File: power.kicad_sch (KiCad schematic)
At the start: 1 part, among them U4 LX7167ACLD-TR

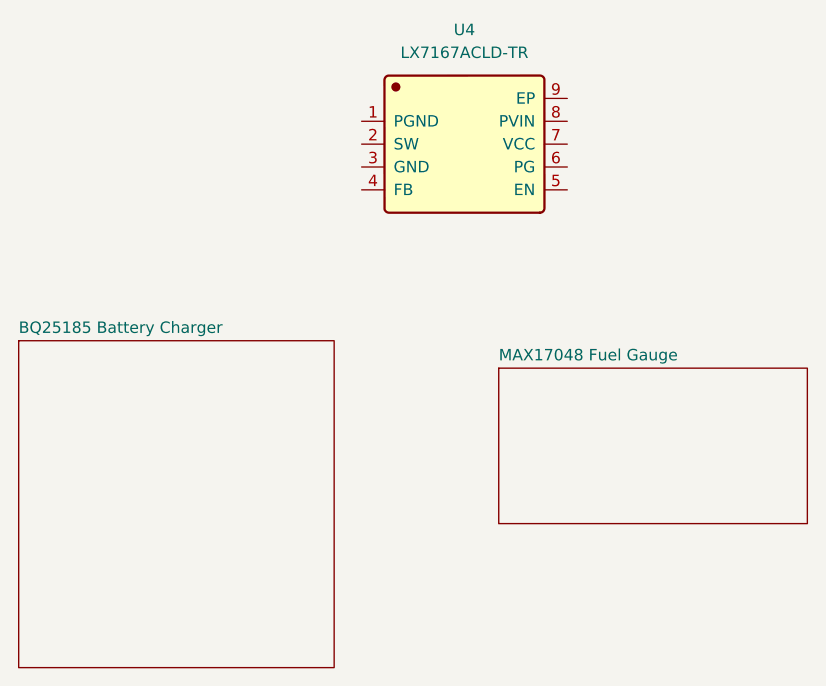
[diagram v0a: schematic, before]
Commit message: Initial design of CS43131 and level shifters
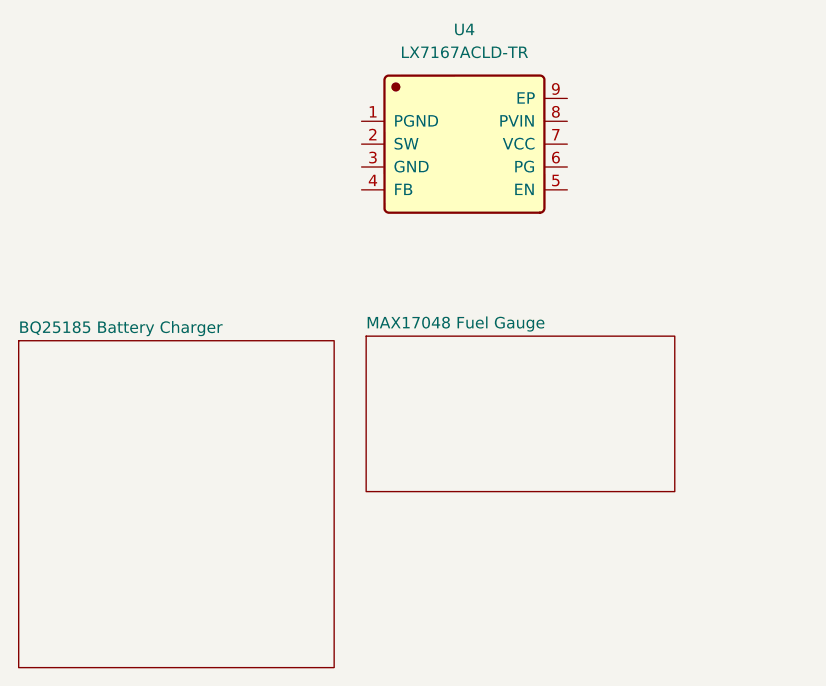
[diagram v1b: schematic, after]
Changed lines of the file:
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@@
 	)
 	(sheet
-		(at 121.92 73.152)
+		(at 107.188 69.596)
 		(size 34.29 17.272)
 		(exclude_from_sim no)
@@
 		)
 		(property "Sheetname" "MAX17048 Fuel Gauge"
-			(at 121.92 72.4404 0)
+			(at 107.188 68.8844 0)
 			(show_name no)
 			(do_not_autoplace no)
@@
 		)
 		(property "Sheetfile" "max17048.kicad_sch"
-			(at 121.92 91.0086 0)
+			(at 107.188 87.4526 0)
 			(hide yes)
 			(show_name no)
